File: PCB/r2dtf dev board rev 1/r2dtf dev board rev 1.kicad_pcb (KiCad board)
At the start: 2 copper layers, 23 parts, among them J1 BATT IN, J10 Power Test Connector, J11 M1 Test Connector, J12 M2 Test Connector, J13 5V Enconder Test Connector, J14 3V3 Enconder Test Connector, J2 Current Sense Jumper Out of b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, J3 Current Sense Jumper Into boa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, J4 Motor 1, J5 Motor 2, J6 M1, J7 BATT OUT, J8 M2, J9 Extra GPIO Test Connector, SW1 External Power Switch, U3 12V to 5V Buck Converter

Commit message: First pass at complete Rev 1. About to quote with JLCPCB
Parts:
- added G***: LOGO, MyFlamingoLogo:flamingo_logo_8-8_6-7, F.Cu at (62.5, 71.0)
- added G***: LOGO, MyFlamingoLogo:flamingo_logo_8-8_6-7, F.Cu at (165.8, 125.3)
- added G***: LOGO, MyFlamingoLogo:flamingo_logo_25_38, B.Cu at (108.3, 94.5)
- added REF**: VIA-0.6 mm, MyConnectors:VIA-0.6 mm, F.Cu at (114.9, 127.6)
- added REF**: VIA-0.6 mm, MyConnectors:VIA-0.6 mm, F.Cu at (54.0, 72.0)
- added REF**: MountingHole_3.2mm_M3, MountingHole:MountingHole_3.2mm_M3, F.Cu at (143.3, 67.2)
- added REF**: MountingHole_3.2mm_M3, MountingHole:MountingHole_3.2mm_M3, F.Cu at (165.5, 131.0)
- added REF**: VIA-0.6 mm, MyConnectors:VIA-0.6 mm, F.Cu at (70.9, 116.0)
- added REF**: VIA-0.6 mm, MyConnectors:VIA-0.6 mm, F.Cu at (155.9, 101.7)
- added REF**: VIA-0.6 mm, MyConnectors:VIA-0.6 mm, F.Cu at (129.6, 62.5)
- added REF**: VIA-0.6 mm, MyConnectors:VIA-0.6 mm, F.Cu at (96.8, 87.0)
- added REF**: VIA-0.6 mm, MyConnectors:VIA-0.6 mm, F.Cu at (80.6, 87.5)
- added REF**: MountingHole_3.2mm_M3, MountingHole:MountingHole_3.2mm_M3, F.Cu at (58.0, 66.0)
- added REF**: VIA-0.6 mm, MyConnectors:VIA-0.6 mm, F.Cu at (60.6, 131.7)
- added REF**: VIA-0.6 mm, MyConnectors:VIA-0.6 mm, F.Cu at (60.5, 104.5)
- added REF**: VIA-0.6 mm, MyConnectors:VIA-0.6 mm, F.Cu at (126.7, 80.8)
- added REF**: VIA-0.6 mm, MyConnectors:VIA-0.6 mm, F.Cu at (140.8, 106.4)
- added REF**: VIA-0.6 mm, MyConnectors:VIA-0.6 mm, F.Cu at (120.6, 121.8)
- added REF**: VIA-0.6 mm, MyConnectors:VIA-0.6 mm, F.Cu at (61.0, 80.9)
- added REF**: MountingHole_3.2mm_M3, MountingHole:MountingHole_3.2mm_M3, F.Cu at (66.5, 108.0)
- added REF**: VIA-0.6 mm, MyConnectors:VIA-0.6 mm, F.Cu at (112.2, 97.9)
- added REF**1: VIA-0.6 mm, MyConnectors:VIA-0.6 mm, F.Cu at (156.9, 101.7)
- added REF**1: VIA-0.6 mm, MyConnectors:VIA-0.6 mm, F.Cu at (130.6, 62.5)
- added REF**1: VIA-0.6 mm, MyConnectors:VIA-0.6 mm, F.Cu at (61.5, 104.5)
- added REF**1: VIA-0.6 mm, MyConnectors:VIA-0.6 mm, F.Cu at (62.0, 80.9)
- added REF**1: VIA-0.6 mm, MyConnectors:VIA-0.6 mm, F.Cu at (81.6, 87.5)
- added REF**1: VIA-0.6 mm, MyConnectors:VIA-0.6 mm, F.Cu at (97.8, 87.0)
- added REF**1: VIA-0.6 mm, MyConnectors:VIA-0.6 mm, F.Cu at (127.7, 80.8)
- added REF**1: VIA-0.6 mm, MyConnectors:VIA-0.6 mm, F.Cu at (113.2, 97.9)
- added REF**1: VIA-0.6 mm, MyConnectors:VIA-0.6 mm, F.Cu at (61.6, 131.7)
- added REF**1: VIA-0.6 mm, MyConnectors:VIA-0.6 mm, F.Cu at (115.9, 127.6)
- added REF**1: VIA-0.6 mm, MyConnectors:VIA-0.6 mm, F.Cu at (121.6, 121.8)
- added REF**1: VIA-0.6 mm, MyConnectors:VIA-0.6 mm, F.Cu at (55.0, 72.0)
- added REF**1: VIA-0.6 mm, MyConnectors:VIA-0.6 mm, F.Cu at (141.8, 106.4)
- added REF**1: VIA-0.6 mm, MyConnectors:VIA-0.6 mm, F.Cu at (71.9, 116.0)
- added REF**2: VIA-0.6 mm, MyConnectors:VIA-0.6 mm, F.Cu at (128.7, 80.8)
- added REF**2: VIA-0.6 mm, MyConnectors:VIA-0.6 mm, F.Cu at (62.6, 131.7)
- added REF**2: VIA-0.6 mm, MyConnectors:VIA-0.6 mm, F.Cu at (72.9, 116.0)
- added REF**2: VIA-0.6 mm, MyConnectors:VIA-0.6 mm, F.Cu at (157.9, 101.7)
- added REF**2: VIA-0.6 mm, MyConnectors:VIA-0.6 mm, F.Cu at (131.6, 62.5)
- added REF**2: VIA-0.6 mm, MyConnectors:VIA-0.6 mm, F.Cu at (63.0, 80.9)
- added REF**2: VIA-0.6 mm, MyConnectors:VIA-0.6 mm, F.Cu at (98.8, 87.0)
- added REF**2: VIA-0.6 mm, MyConnectors:VIA-0.6 mm, F.Cu at (116.9, 127.6)
- added REF**2: VIA-0.6 mm, MyConnectors:VIA-0.6 mm, F.Cu at (56.0, 72.0)
- added REF**2: VIA-0.6 mm, MyConnectors:VIA-0.6 mm, F.Cu at (82.6, 87.5)
- added REF**2: VIA-0.6 mm, MyConnectors:VIA-0.6 mm, F.Cu at (122.6, 121.8)
- added REF**2: VIA-0.6 mm, MyConnectors:VIA-0.6 mm, F.Cu at (142.8, 106.4)
- added REF**2: VIA-0.6 mm, MyConnectors:VIA-0.6 mm, F.Cu at (62.5, 104.5)
- added REF**2: VIA-0.6 mm, MyConnectors:VIA-0.6 mm, F.Cu at (114.2, 97.9)
- added REF**3: VIA-0.6 mm, MyConnectors:VIA-0.6 mm, F.Cu at (60.5, 105.5)
- added REF**3: VIA-0.6 mm, MyConnectors:VIA-0.6 mm, F.Cu at (114.9, 128.6)
- added REF**3: VIA-0.6 mm, MyConnectors:VIA-0.6 mm, F.Cu at (70.9, 117.0)
- added REF**3: VIA-0.6 mm, MyConnectors:VIA-0.6 mm, F.Cu at (112.2, 98.9)
- added REF**3: VIA-0.6 mm, MyConnectors:VIA-0.6 mm, F.Cu at (54.0, 73.0)
- added REF**3: VIA-0.6 mm, MyConnectors:VIA-0.6 mm, F.Cu at (60.6, 132.7)
- added REF**3: VIA-0.6 mm, MyConnectors:VIA-0.6 mm, F.Cu at (126.7, 81.8)
- added REF**3: VIA-0.6 mm, MyConnectors:VIA-0.6 mm, F.Cu at (155.9, 102.7)
- added REF**3: VIA-0.6 mm, MyConnectors:VIA-0.6 mm, F.Cu at (140.8, 107.4)
- added REF**3: VIA-0.6 mm, MyConnectors:VIA-0.6 mm, F.Cu at (96.8, 88.0)
- added REF**3: VIA-0.6 mm, MyConnectors:VIA-0.6 mm, F.Cu at (61.0, 81.9)
- added REF**3: VIA-0.6 mm, MyConnectors:VIA-0.6 mm, F.Cu at (80.6, 88.5)
- added REF**3: VIA-0.6 mm, MyConnectors:VIA-0.6 mm, F.Cu at (129.6, 63.5)
- added REF**3: VIA-0.6 mm, MyConnectors:VIA-0.6 mm, F.Cu at (120.6, 122.8)
- added REF**4: VIA-0.6 mm, MyConnectors:VIA-0.6 mm, F.Cu at (141.8, 107.4)
- added REF**4: VIA-0.6 mm, MyConnectors:VIA-0.6 mm, F.Cu at (55.0, 73.0)
- added REF**4: VIA-0.6 mm, MyConnectors:VIA-0.6 mm, F.Cu at (62.0, 81.9)
- added REF**4: VIA-0.6 mm, MyConnectors:VIA-0.6 mm, F.Cu at (61.6, 132.7)
- added REF**4: VIA-0.6 mm, MyConnectors:VIA-0.6 mm, F.Cu at (71.9, 117.0)
- added REF**4: VIA-0.6 mm, MyConnectors:VIA-0.6 mm, F.Cu at (156.9, 102.7)
- added REF**4: VIA-0.6 mm, MyConnectors:VIA-0.6 mm, F.Cu at (121.6, 122.8)
- added REF**4: VIA-0.6 mm, MyConnectors:VIA-0.6 mm, F.Cu at (115.9, 128.6)
- added REF**4: VIA-0.6 mm, MyConnectors:VIA-0.6 mm, F.Cu at (130.6, 63.5)
- added REF**4: VIA-0.6 mm, MyConnectors:VIA-0.6 mm, F.Cu at (61.5, 105.5)
- added REF**4: VIA-0.6 mm, MyConnectors:VIA-0.6 mm, F.Cu at (81.6, 88.5)
- added REF**4: VIA-0.6 mm, MyConnectors:VIA-0.6 mm, F.Cu at (113.2, 98.9)
- added REF**4: VIA-0.6 mm, MyConnectors:VIA-0.6 mm, F.Cu at (127.7, 81.8)
- added REF**4: VIA-0.6 mm, MyConnectors:VIA-0.6 mm, F.Cu at (97.8, 88.0)
- added REF**5: VIA-0.6 mm, MyConnectors:VIA-0.6 mm, F.Cu at (62.5, 105.5)
- added REF**5: VIA-0.6 mm, MyConnectors:VIA-0.6 mm, F.Cu at (114.2, 98.9)
- added REF**5: VIA-0.6 mm, MyConnectors:VIA-0.6 mm, F.Cu at (122.6, 122.8)
- added REF**5: VIA-0.6 mm, MyConnectors:VIA-0.6 mm, F.Cu at (128.7, 81.8)
- added REF**5: VIA-0.6 mm, MyConnectors:VIA-0.6 mm, F.Cu at (142.8, 107.4)
- added REF**5: VIA-0.6 mm, MyConnectors:VIA-0.6 mm, F.Cu at (131.6, 63.5)
- added REF**5: VIA-0.6 mm, MyConnectors:VIA-0.6 mm, F.Cu at (56.0, 73.0)
- added REF**5: VIA-0.6 mm, MyConnectors:VIA-0.6 mm, F.Cu at (157.9, 102.7)
- added REF**5: VIA-0.6 mm, MyConnectors:VIA-0.6 mm, F.Cu at (72.9, 117.0)
- added REF**5: VIA-0.6 mm, MyConnectors:VIA-0.6 mm, F.Cu at (63.0, 81.9)
- added REF**5: VIA-0.6 mm, MyConnectors:VIA-0.6 mm, F.Cu at (62.6, 132.7)
- added REF**5: VIA-0.6 mm, MyConnectors:VIA-0.6 mm, F.Cu at (116.9, 128.6)
- added REF**5: VIA-0.6 mm, MyConnectors:VIA-0.6 mm, F.Cu at (82.6, 88.5)
- added REF**5: VIA-0.6 mm, MyConnectors:VIA-0.6 mm, F.Cu at (98.8, 88.0)
- added REF**6: VIA-0.6 mm, MyConnectors:VIA-0.6 mm, F.Cu at (163.2, 84.4)
- added REF**6: VIA-0.6 mm, MyConnectors:VIA-0.6 mm, F.Cu at (90.5, 114.6)
- added REF**6: VIA-0.6 mm, MyConnectors:VIA-0.6 mm, F.Cu at (81.5, 132.5)
- added REF**6: VIA-0.6 mm, MyConnectors:VIA-0.6 mm, F.Cu at (163.2, 69.2)
- added REF**6: VIA-0.6 mm, MyConnectors:VIA-0.6 mm, F.Cu at (60.5, 106.5)
- added REF**6: VIA-0.6 mm, MyConnectors:VIA-0.6 mm, F.Cu at (169.0, 69.2)
- added REF**6: VIA-0.6 mm, MyConnectors:VIA-0.6 mm, F.Cu at (140.9, 74.0)
- added REF**6: VIA-0.6 mm, MyConnectors:VIA-0.6 mm, F.Cu at (137.2, 64.4)
- added REF**6: VIA-0.6 mm, MyConnectors:VIA-0.6 mm, F.Cu at (163.2, 66.6)
- added REF**6: VIA-0.6 mm, MyConnectors:VIA-0.6 mm, F.Cu at (114.9, 129.6)
- added REF**6: VIA-0.6 mm, MyConnectors:VIA-0.6 mm, F.Cu at (169.0, 81.8)
- added REF**6: VIA-0.6 mm, MyConnectors:VIA-0.6 mm, F.Cu at (68.2, 132.0)
- added REF**6: VIA-0.6 mm, MyConnectors:VIA-0.6 mm, F.Cu at (89.5, 106.0)
- added REF**6: VIA-0.6 mm, MyConnectors:VIA-0.6 mm, F.Cu at (81.5, 125.4)
- added REF**6: VIA-0.6 mm, MyConnectors:VIA-0.6 mm, F.Cu at (70.9, 118.0)
- added REF**6: VIA-0.6 mm, MyConnectors:VIA-0.6 mm, F.Cu at (140.8, 108.4)
- added REF**6: VIA-0.6 mm, MyConnectors:VIA-0.6 mm, F.Cu at (147.7, 61.3)
- added REF**6: VIA-0.6 mm, MyConnectors:VIA-0.6 mm, F.Cu at (105.5, 98.9)
- added REF**6: VIA-0.6 mm, MyConnectors:VIA-0.6 mm, F.Cu at (112.2, 99.9)
- added REF**6: VIA-0.6 mm, MyConnectors:VIA-0.6 mm, F.Cu at (150.3, 64.4)
- added REF**6: VIA-0.6 mm, MyConnectors:VIA-0.6 mm, F.Cu at (56.2, 109.3)
- added REF**6: VIA-0.6 mm, MyConnectors:VIA-0.6 mm, F.Cu at (163.2, 79.3)
- added REF**6: VIA-0.6 mm, MyConnectors:VIA-0.6 mm, F.Cu at (60.8, 116.8)
- added REF**6: VIA-0.6 mm, MyConnectors:VIA-0.6 mm, F.Cu at (97.7, 65.7)
- added REF**6: VIA-0.6 mm, MyConnectors:VIA-0.6 mm, F.Cu at (152.1, 126.2)
- added REF**6: VIA-0.6 mm, MyConnectors:VIA-0.6 mm, F.Cu at (54.0, 74.0)
- added REF**6: VIA-0.6 mm, MyConnectors:VIA-0.6 mm, F.Cu at (155.9, 103.7)
- added REF**6: VIA-0.6 mm, MyConnectors:VIA-0.6 mm, F.Cu at (78.0, 68.2)
- added REF**6: VIA-0.6 mm, MyConnectors:VIA-0.6 mm, F.Cu at (57.2, 119.8)
- added REF**6: VIA-0.6 mm, MyConnectors:VIA-0.6 mm, F.Cu at (72.2, 130.4)
- added REF**6: VIA-0.6 mm, MyConnectors:VIA-0.6 mm, F.Cu at (129.6, 64.5)
- added REF**6: VIA-0.6 mm, MyConnectors:VIA-0.6 mm, F.Cu at (128.6, 73.7)
- added REF**6: VIA-0.6 mm, MyConnectors:VIA-0.6 mm, F.Cu at (114.7, 81.8)
- added REF**6: VIA-0.6 mm, MyConnectors:VIA-0.6 mm, F.Cu at (163.2, 71.6)
- added REF**6: VIA-0.6 mm, MyConnectors:VIA-0.6 mm, F.Cu at (86.7, 111.2)
- added REF**6: VIA-0.6 mm, MyConnectors:VIA-0.6 mm, F.Cu at (67.7, 70.3)
- added REF**6: VIA-0.6 mm, MyConnectors:VIA-0.6 mm, F.Cu at (60.6, 133.7)
- added REF**6: VIA-0.6 mm, MyConnectors:VIA-0.6 mm, F.Cu at (82.2, 111.2)
- added REF**6: VIA-0.6 mm, MyConnectors:VIA-0.6 mm, F.Cu at (95.1, 61.3)
- added REF**6: VIA-0.6 mm, MyConnectors:VIA-0.6 mm, F.Cu at (80.6, 89.5)
- added REF**6: VIA-0.6 mm, MyConnectors:VIA-0.6 mm, F.Cu at (126.7, 82.8)
- added REF**6: VIA-0.6 mm, MyConnectors:VIA-0.6 mm, F.Cu at (81.5, 128.0)
- added REF**6: VIA-0.6 mm, MyConnectors:VIA-0.6 mm, F.Cu at (163.2, 76.7)
- added REF**6: VIA-0.6 mm, MyConnectors:VIA-0.6 mm, F.Cu at (80.1, 62.3)
- added REF**6: VIA-0.6 mm, MyConnectors:VIA-0.6 mm, F.Cu at (163.2, 64.1)
- added REF**6: VIA-0.6 mm, MyConnectors:VIA-0.6 mm, F.Cu at (64.4, 119.7)
- added REF**6: VIA-0.6 mm, MyConnectors:VIA-0.6 mm, F.Cu at (124.3, 128.0)
- added REF**6: VIA-0.6 mm, MyConnectors:VIA-0.6 mm, F.Cu at (55.0, 62.3)
- added REF**6: VIA-0.6 mm, MyConnectors:VIA-0.6 mm, F.Cu at (163.2, 81.8)
- added REF**6: VIA-0.6 mm, MyConnectors:VIA-0.6 mm, F.Cu at (120.6, 123.8)
- added REF**6: VIA-0.6 mm, MyConnectors:VIA-0.6 mm, F.Cu at (61.0, 82.9)
- added REF**6: VIA-0.6 mm, MyConnectors:VIA-0.6 mm, F.Cu at (81.5, 122.7)
- added REF**6: VIA-0.6 mm, MyConnectors:VIA-0.6 mm, F.Cu at (123.5, 112.6)
- added REF**6: VIA-0.6 mm, MyConnectors:VIA-0.6 mm, F.Cu at (54.5, 98.1)
- added REF**6: VIA-0.6 mm, MyConnectors:VIA-0.6 mm, F.Cu at (96.8, 89.0)
- added REF**7: VIA-0.6 mm, MyConnectors:VIA-0.6 mm, F.Cu at (71.9, 118.0)
- added REF**7: VIA-0.6 mm, MyConnectors:VIA-0.6 mm, F.Cu at (141.8, 108.4)
- added REF**7: VIA-0.6 mm, MyConnectors:VIA-0.6 mm, F.Cu at (55.0, 74.0)
- added REF**7: VIA-0.6 mm, MyConnectors:VIA-0.6 mm, F.Cu at (81.6, 89.5)
- added REF**7: VIA-0.6 mm, MyConnectors:VIA-0.6 mm, F.Cu at (62.0, 82.9)
- added REF**7: VIA-0.6 mm, MyConnectors:VIA-0.6 mm, F.Cu at (113.2, 99.9)
- added REF**7: VIA-0.6 mm, MyConnectors:VIA-0.6 mm, F.Cu at (61.6, 133.7)
- added REF**7: VIA-0.6 mm, MyConnectors:VIA-0.6 mm, F.Cu at (127.7, 82.8)
- added REF**7: VIA-0.6 mm, MyConnectors:VIA-0.6 mm, F.Cu at (61.5, 106.5)
- added REF**7: VIA-0.6 mm, MyConnectors:VIA-0.6 mm, F.Cu at (97.8, 89.0)
- added REF**7: VIA-0.6 mm, MyConnectors:VIA-0.6 mm, F.Cu at (130.6, 64.5)
- added REF**7: VIA-0.6 mm, MyConnectors:VIA-0.6 mm, F.Cu at (121.6, 123.8)
- added REF**7: VIA-0.6 mm, MyConnectors:VIA-0.6 mm, F.Cu at (115.9, 129.6)
- added REF**7: VIA-0.6 mm, MyConnectors:VIA-0.6 mm, F.Cu at (156.9, 103.7)
- added REF**8: VIA-0.6 mm, MyConnectors:VIA-0.6 mm, F.Cu at (142.3, 93.6)
- added REF**8: VIA-0.6 mm, MyConnectors:VIA-0.6 mm, F.Cu at (63.0, 82.9)
- added REF**8: VIA-0.6 mm, MyConnectors:VIA-0.6 mm, F.Cu at (114.2, 99.9)
- added REF**8: VIA-0.6 mm, MyConnectors:VIA-0.6 mm, F.Cu at (95.6, 114.5)
- added REF**8: VIA-0.6 mm, MyConnectors:VIA-0.6 mm, F.Cu at (98.8, 89.0)
- added REF**8: VIA-0.6 mm, MyConnectors:VIA-0.6 mm, F.Cu at (142.8, 108.4)
- added REF**8: VIA-0.6 mm, MyConnectors:VIA-0.6 mm, F.Cu at (72.9, 118.0)
- added REF**8: VIA-0.6 mm, MyConnectors:VIA-0.6 mm, F.Cu at (82.6, 89.5)
- added REF**8: VIA-0.6 mm, MyConnectors:VIA-0.6 mm, F.Cu at (131.6, 64.5)
- added REF**8: VIA-0.6 mm, MyConnectors:VIA-0.6 mm, F.Cu at (163.2, 74.2)
- added REF**8: VIA-0.6 mm, MyConnectors:VIA-0.6 mm, F.Cu at (116.9, 129.6)
- added REF**8: VIA-0.6 mm, MyConnectors:VIA-0.6 mm, F.Cu at (122.6, 123.8)
- added REF**8: VIA-0.6 mm, MyConnectors:VIA-0.6 mm, F.Cu at (62.5, 106.5)
- added REF**8: VIA-0.6 mm, MyConnectors:VIA-0.6 mm, F.Cu at (62.6, 133.7)
- added REF**8: VIA-0.6 mm, MyConnectors:VIA-0.6 mm, F.Cu at (56.0, 74.0)
- added REF**8: VIA-0.6 mm, MyConnectors:VIA-0.6 mm, F.Cu at (128.7, 82.8)
- added REF**8: VIA-0.6 mm, MyConnectors:VIA-0.6 mm, F.Cu at (157.9, 103.7)
- added REF**8: VIA-0.6 mm, MyConnectors:VIA-0.6 mm, F.Cu at (129.8, 93.6)
- added REF**8: VIA-0.6 mm, MyConnectors:VIA-0.6 mm, F.Cu at (125.4, 93.6)
- added REF**8: VIA-0.6 mm, MyConnectors:VIA-0.6 mm, F.Cu at (133.9, 122.3)
- moved J14 27.0 mm to (76.6, 120.0), turned to -90 degrees
- moved J10 23.2 mm to (58.0, 106.6)
- moved C4 15.3 mm to (70.0, 122.5), turned to 180 degrees
- moved J9 14.1 mm to (143.5, 119.5)
- moved XA1 13.8 mm to (96.5, 124.9)
- moved U1 12.4 mm to (67.0, 126.8), turned to 0 degrees
- moved U3 12.0 mm to (147.0, 115.2)
- moved J5 11.6 mm to (87.7, 65.7)
- moved C2 10.4 mm to (85.0, 71.7)
- moved C3 9.64 mm to (63.8, 122.5), turned to 0 degrees
- moved C1 9.39 mm to (77.1, 104.9), turned to 0 degrees
- moved J2 8.58 mm to (88.7, 114.7)
- moved J3 8.58 mm to (88.7, 119.0)
- moved J13 6.23 mm to (58.0, 121.5), turned to -90 degrees
- moved J4 4.50 mm to (74.9, 108.7), turned to 90 degrees
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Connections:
- net Net-(J1-Pin_2-GND) renamed /BATT GND
- net Net-(J3-Pin_1) renamed /Post-Jumper CS1
- net Net-(J3-Pin_2) renamed /Post-Jumper CS2
- net Net-(J4-M1-Black-Power) renamed /M1 Black
- net Net-(J4-M1-Red-Power) renamed /M1 Red
- net Net-(J5-M2-Black-Power) renamed /M2 Black
- net Net-(J5-M2-Red-Power) renamed /M2 Red
- net Net-(J7-Pin_2-VBAT) renamed /BATT POST_SWITCH
- net Net-(J9-Pin_1) renamed /D3
- net Net-(J9-Pin_2) renamed /D11
- net Net-(J9-Pin_3) renamed /D13
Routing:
- net +5V: track 0.00 -> 226.5 mm, vias 0 -> 4
- net +3V3: track 0.00 -> 156.6 mm, vias 0 -> 4
- net M2_CS: track 0.00 -> 103.7 mm
- net M1_CS: track 0.00 -> 96.7 mm
- net M2-Enc_B-White-5V: track 0.00 -> 87.5 mm
- net M2_PWM: track 0.00 -> 86.2 mm, vias 0 -> 2
- net M2_EN/DIAG: track 0.00 -> 84.9 mm, vias 0 -> 4
- net M2-Enc_A-Yellow-5V: track 0.00 -> 83.6 mm
- net M2_INB: track 0.00 -> 80.7 mm, vias 0 -> 2
- net M1_PWM: track 0.00 -> 76.4 mm, vias 0 -> 2
- net M2_INA: track 0.00 -> 76.0 mm, vias 0 -> 2
- net M1_EN/DIAG: track 0.00 -> 67.1 mm, vias 0 -> 2
- net M1_INB: track 0.00 -> 64.8 mm
- net TXU_OE: track 0.00 -> 64.1 mm, vias 0 -> 2
- net M1-Enc_B-White-3V3: track 0.00 -> 60.3 mm, vias 0 -> 2
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- added copper zone on B.Cu, net /BATT GND
- added copper zone on F.Cu, net /BATT GND
- added copper zone on B.Cu, net /BATT POST_SWITCH
- added copper zone on F.Cu, net /BATT POST_SWITCH
- added copper zone on B.Cu, net /M1 Black
- added copper zone on F.Cu, net /M1 Black
- added copper zone on B.Cu, net /M1 Red
- added copper zone on F.Cu, net /M1 Red
- added copper zone on B.Cu, net /M2 Black
- added copper zone on F.Cu, net /M2 Black
- added copper zone on B.Cu, net /M2 Red
- added copper zone on F.Cu, net /M2 Red
- added copper zone on B.Cu, net GND
- added copper zone on F.Cu, net GND
- added copper zone on B.Cu, net VBAT
- added copper zone on F.Cu, net VBAT
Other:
- board outline added: 118 x 75.6 mm
- board text added: "1END"
- board text added: "1INA"
- board text added: "1INB"
- board text added: "1PWM"
- board text added: "2END"
- board text added: "2INA"
- board text added: "2INB"
- board text added: "2PWM"
- board text added: "3V3"
- board text added: "5V"
- board text added: "5V/Blue"
- board text added: "BATT+"
- board text added: "BATT-"
- board text added: "Bk"
- board text added: "Blue"
- board text added: "CS1"
- board text added: "CS2"
- board text added: "Curr Sense 144 mV/A"
- board text added: "D11"
- board text added: "D13"
- board text added: "D3"
- board text added: "Dev Board for [Rev 1] Pololu Dual VNH5019 Motor Driver GitHub: @individual61 Jan 2024"
- board text added: "Dev Board for [Rev 1] Pololu Dual VNH5019 Motor Driver GitHub: @individual61 Paul Blackburn January 2024"
- board text added: "ENCA/Y"
- board text added: "ENCB/W"
- board text added: "Encoder 3V3"
- board text added: "Encoder 5 V"
- board text added: "GND"
- board text added: "GND/Green"
- board text added: "GPIO"
- board text added: "Grn"
- board text added: "M/BK"
- board text added: "M/Red"
- board text added: "M1A"
- board text added: "M1B"
- board text added: "M1CS"
- board text added: "M2A"
- board text added: "M2B"
- board text added: "M2CS"
- board text added: "Motor 1 Connector"
- board text added: "Motor 2 Connector"
- board text added: "Red"
- board text added: "TXU0104 OE"
- board text added: "VBAT"
- board text added: "Wh"
- board text added: "Wire Connections"
- board text added: "Y"

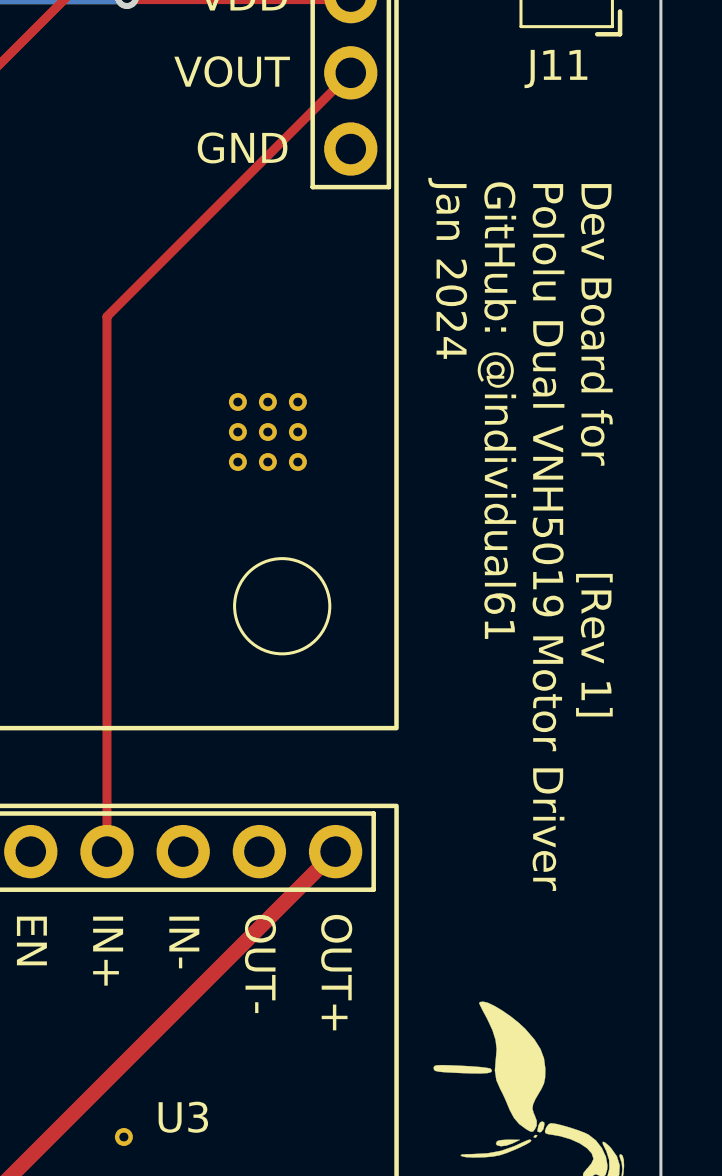
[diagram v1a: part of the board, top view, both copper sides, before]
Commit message: Removed thermal reliefs on high current pours
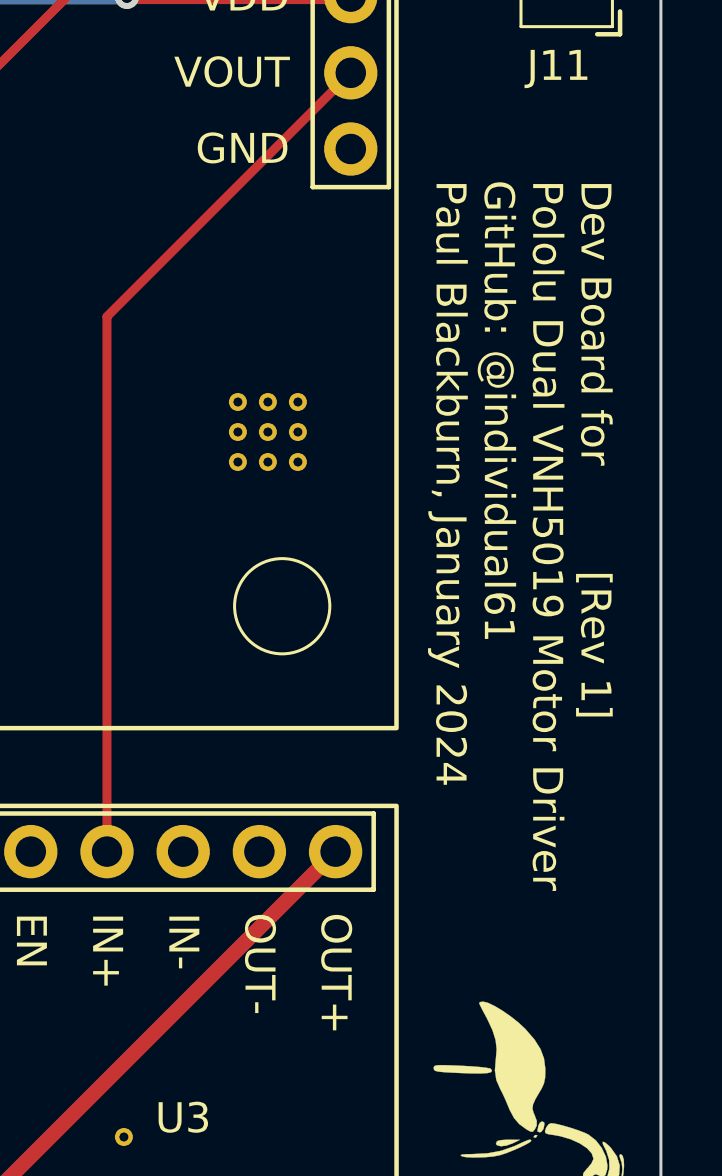
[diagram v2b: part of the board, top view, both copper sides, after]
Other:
- board text added: "Dev Board for [Rev 1] Pololu Dual VNH5019 Motor Driver GitHub: @individual61 Paul Blackburn, January 2024"
- board text removed: "Dev Board for [Rev 1] Pololu Dual VNH5019 Motor Driver GitHub: @individual61 Jan 2024"
- board text removed: "Dev Board for [Rev 1] Pololu Dual VNH5019 Motor Driver GitHub: @individual61 Paul Blackburn January 2024"
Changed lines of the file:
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@@
       (plot_on_all_layers_selection 0x0000000_00000000)
       (disableapertmacros false)
-      (usegerberextensions false)
+      (usegerberextensions true)
       (usegerberattributes true)
       (usegerberadvancedattributes true)
-      (creategerberjobfile true)
+      (creategerberjobfile false)
       (dashed_line_dash_ratio 12.000000)
       (dashed_line_gap_ratio 3.000000)
@@
       (plotinvisibletext false)
       (sketchpadsonfab false)
-      (subtractmaskfromsilk false)
+      (subtractmaskfromsilk true)
       (outputformat 1)
       (mirror false)
-      (drillshape 1)
+      (drillshape 0)
       (scaleselection 1)
-      (outputdirectory "")
+      (outputdirectory "Manufacturing files/Rev 1 FIrst Quote/")
     )
   )
@@
       (stroke (width 0.15) (type default)) (fill none) (layer "F.Fab"))
     (pad "1" thru_hole circle (at 0 0 90) (size 2 2) (drill 1.3) (layers "*.Cu" "*.Mask")
-      (net 51 "/M1 Red") (pinfunction "Pin_1") (pintype "passive"))
+      (net 51 "/M1 Red") (pinfunction "Pin_1") (pintype "passive") (zone_connect 2))
     (pad "2" thru_hole circle (at 5 0 90) (size 2 2) (drill 1.3) (layers "*.Cu" "*.Mask")
-      (net 52 "/M1 Black") (pinfunction "Pin_2") (pintype "passive"))
+      (net 52 "/M1 Black") (pinfunction "Pin_2") (pintype "passive") (zone_connect 2))
     (model "${KICAD_USER_LIBRARY}/3D Models/Degson Screw Terminal 2P 5 mm DG301-5.0-02P-12-00AH.STEP"
       (offset (xyz -2.5 4.5 0))
@@
       (stroke (width 0.15) (type default)) (fill none) (layer "F.Fab"))
     (pad "1" thru_hole circle (at 0 0 90) (size 2 2) (drill 1.3) (layers "*.Cu" "*.Mask")
-      (net 54 "/M2 Red") (pinfunction "Pin_1") (pintype "passive"))
+      (net 54 "/M2 Red") (pinfunction "Pin_1") (pintype "passive") (zone_connect 2))
     (pad "2" thru_hole circle (at 5 0 90) (size 2 2) (drill 1.3) (layers "*.Cu" "*.Mask")
-      (net 53 "/M2 Black") (pinfunction "Pin_2") (pintype "passive"))
+      (net 53 "/M2 Black") (pinfunction "Pin_2") (pintype "passive") (zone_connect 2))
     (model "${KICAD_USER_LIBRARY}/3D Models/Degson Screw Terminal 2P 5 mm DG301-5.0-02P-12-00AH.STEP"
       (offset (xyz -2.5 4.5 0))
@@
       (stroke (width 0.15) (type default)) (fill none) (layer "F.Fab"))
     (pad "1" thru_hole circle (at 0 0 90) (size 2 2) (drill 1.3) (layers "*.Cu" "*.Mask")
-      (net 47 "/BATT GND") (pinfunction "Pin_1-GND") (pintype "passive"))
+      (net 47 "/BATT GND") (pinfunction "Pin_1-GND") (pintype "passive") (zone_connect 2))
     (pad "2" thru_hole circle (at 5 0 90) (size 2 2) (drill 1.3) (layers "*.Cu" "*.Mask")
-      (net 48 "/BATT POST_SWITCH") (pinfunction "Pin_2-VBAT") (pintype "passive"))
+      (net 48 "/BATT POST_SWITCH") (pinfunction "Pin_2-VBAT") (pintype "passive") (zone_connect 2))
     (model "${KICAD_USER_LIBRARY}/3D Models/Degson Screw Terminal 2P 5 mm DG301-5.0-02P-12-00AH.STEP"
       (offset (xyz -2.5 4.5 0))
@@
   (gr_arc (start 170 133.585786) (mid 169.414214 135) (end 168 135.585786)
     (stroke (width 0.1) (type default)) (layer "Edge.Cuts"))
-  (gr_text "Dev Board for        [Rev 1]\nPololu Dual VNH5019 Motor Driver\nGitHub: @individual61\nPaul Blackburn January 2024" (at 117.2 68.9) (layer "B.SilkS")
+  (gr_text "Dev Board for        [Rev 1]\nPololu Dual VNH5019 Motor Driver\nGitHub: @individual61\nPaul Blackburn, January 2024" (at 117.2 68.9) (layer "B.SilkS")
     (effects (font (size 1 1) (thickness 0.153)) (justify left top mirror))
   )
@@
     (effects (font (size 1 1) (thickness 0.153)))
   )
-  (gr_text "Dev Board for        [Rev 1]\nPololu Dual VNH5019 Motor Driver\nGitHub: @individual61\nJan 2024" (at 168.4 94.3 270) (layer "F.SilkS")
+  (gr_text "Dev Board for        [Rev 1]\nPololu Dual VNH5019 Motor Driver\nGitHub: @individual61\nPaul Blackburn, January 2024" (at 168.4 94.3 270) (layer "F.SilkS")
     (effects (font (size 1 1) (thickness 0.153)) (justify left top))
   )
